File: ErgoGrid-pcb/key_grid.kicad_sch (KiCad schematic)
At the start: 0 parts

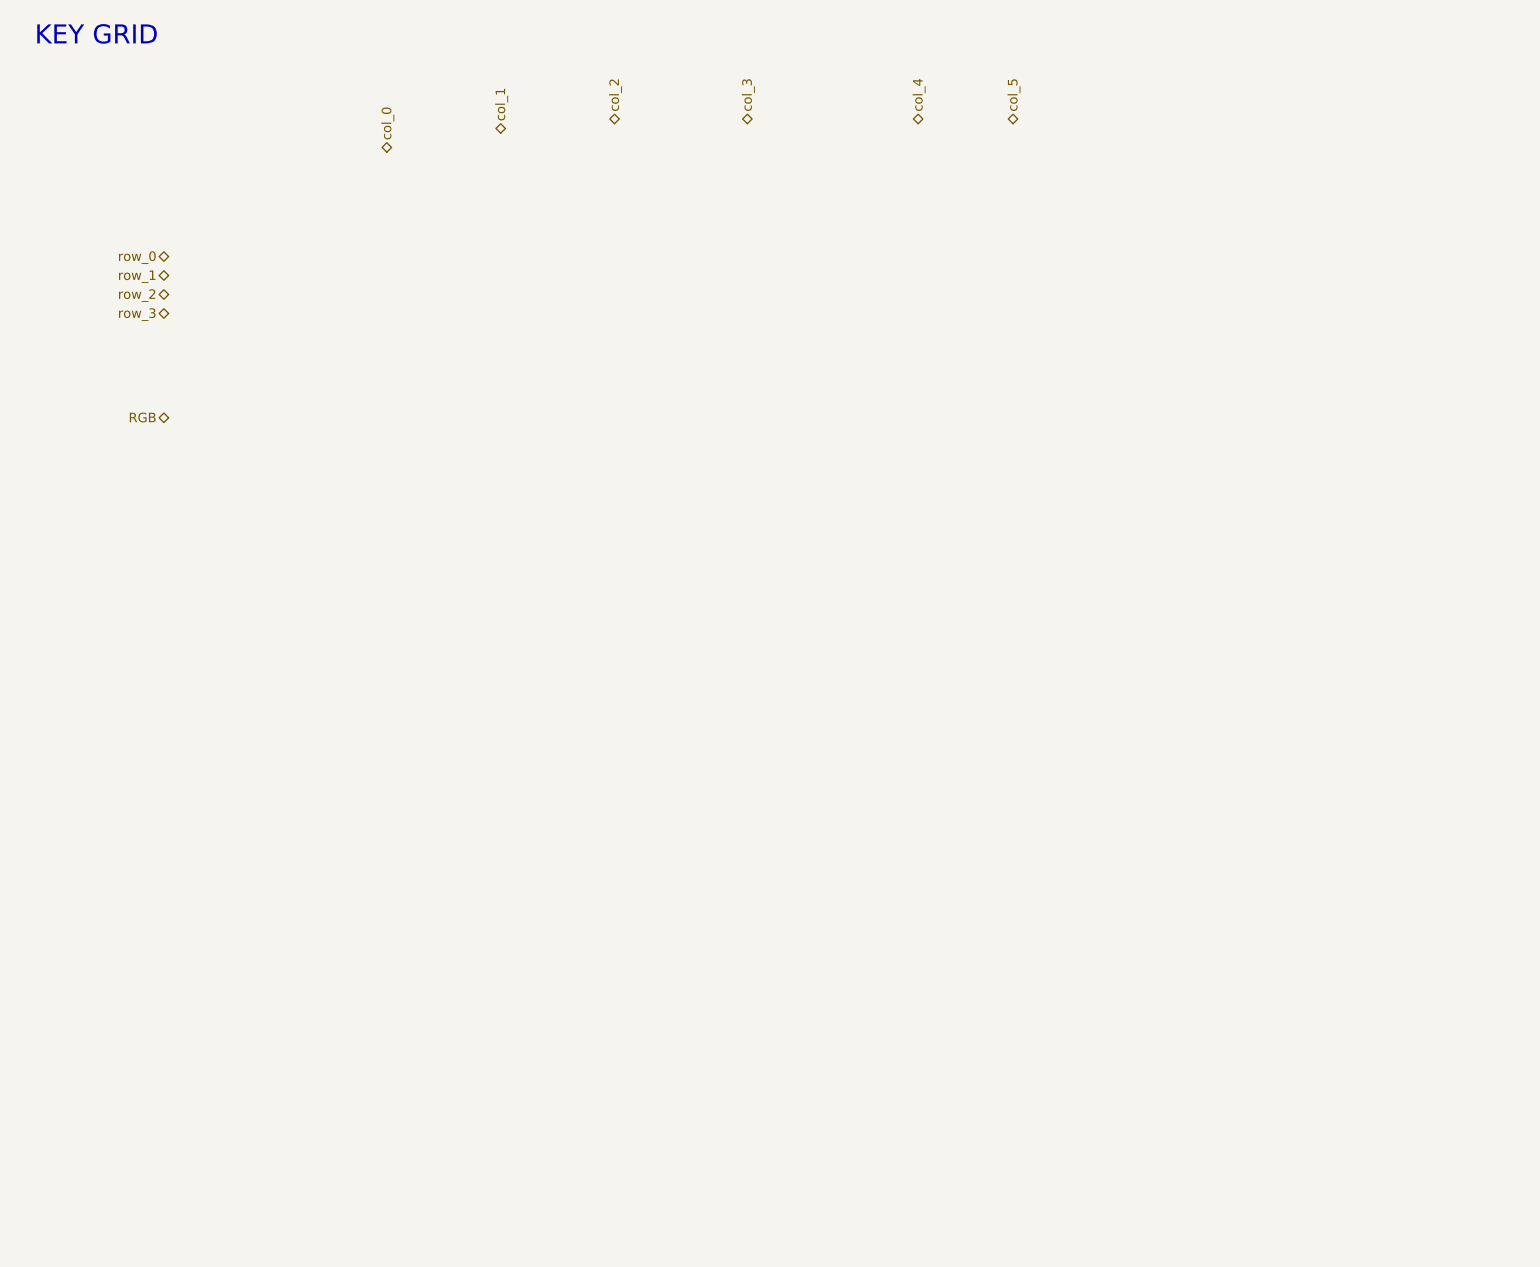
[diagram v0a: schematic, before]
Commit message: pcb: add key and RGB grids to schematic
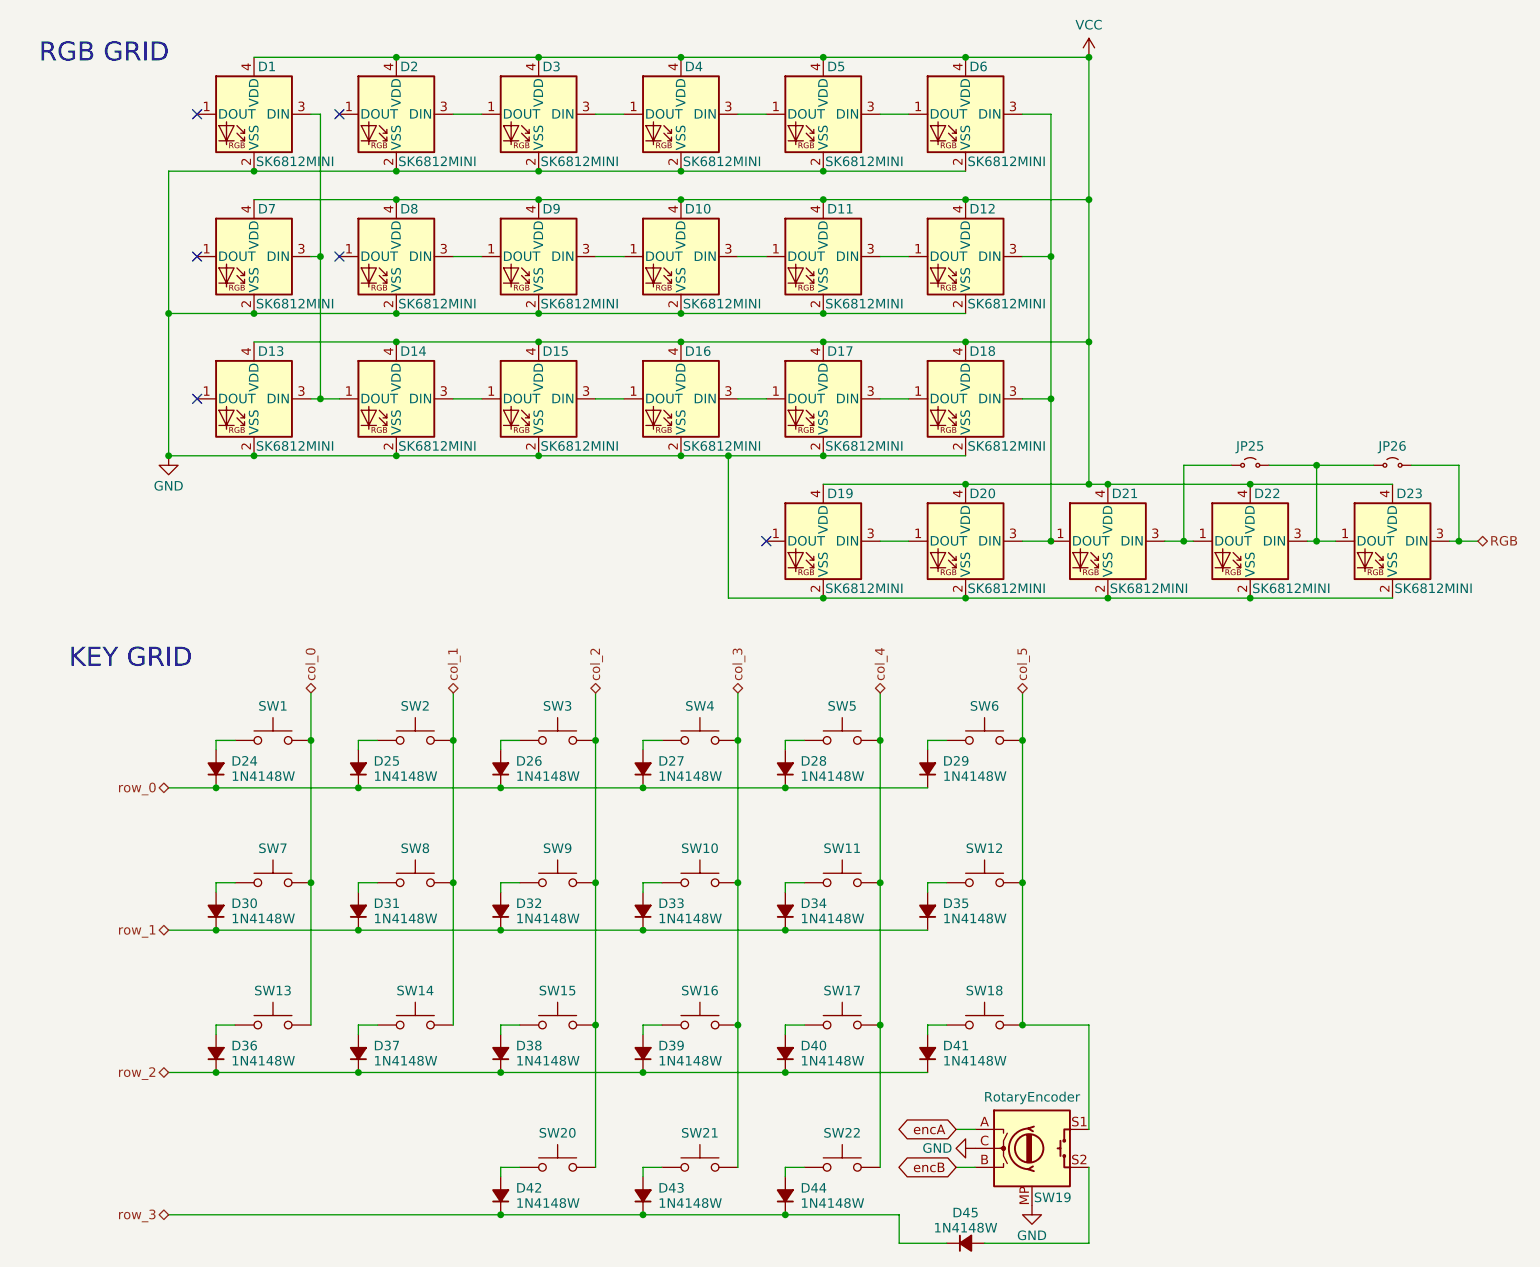
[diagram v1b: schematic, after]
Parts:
- added D1, D10, D11, D12, D13, D14, D15, D16, D17, D18, D19, D2, D20, D21, D22, D23, D3, D4, D5, D6, D7, D8, D9: SK6812MINI, LED_SMD:LED_SK6812MINI_PLCC4_3.5x3.5mm_P1.75mm, symbol SK6812MINI:SK6812MINI
- added D24, D25, D26, D27, D28, D29, D30, D31, D32, D33, D34, D35, D36, D37, D38, D39, D40, D41, D42, D43, D44, D45: 1N4148W, symbol D_Small_Filled:D_Small_Filled
- added JP25: EncBot, symbol Jumper_2_Small_Open:Jumper_2_Small_Open
- added JP26: EncTop, symbol Jumper_2_Small_Open:Jumper_2_Small_Open
- added SW1, SW10, SW11, SW12, SW13, SW14, SW15, SW16, SW17, SW18, SW2, SW20, SW21, SW22, SW3, SW4, SW5, SW6, SW7, SW8, SW9: SW_Push, symbol SW_Push:SW_Push
- added SW19: RotaryEncoder, symbol RotaryEncoder_Switch_MP:RotaryEncoder_Switch_MP
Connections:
- net RGB: now also D23.3 (DIN), JP26.2 (B)
- net col_0: now also SW1.2, SW13.2, SW7.2
- net col_1: now also SW14.2, SW2.2, SW8.2
- net col_2: now also SW15.2, SW20.2, SW3.2, SW9.2
- net col_3: now also SW10.2, SW16.2, SW21.2, SW4.2
- net col_4: now also SW11.2, SW17.2, SW22.2, SW5.2
- net col_5: now also SW12.2, SW18.2, SW19.S1, SW6.2
- net row_0: now also D24.1 (K), D25.1 (K), D26.1 (K), D27.1 (K), D28.1 (K), D29.1 (K)
- net row_1: now also D30.1 (K), D31.1 (K), D32.1 (K), D33.1 (K), D34.1 (K), D35.1 (K)
- net row_2: now also D36.1 (K), D37.1 (K), D38.1 (K), D39.1 (K), D40.1 (K), D41.1 (K)
- net row_3: now also D42.1 (K), D43.1 (K), D44.1 (K), D45.1 (K)
- new net: D22.3 (DIN), D23.1 (DOUT), JP25.2 (B), JP26.1 (A)
- new net: D33.2 (A), SW10.1
- new net: D45.2 (A), SW19.S2
- new net: D17.3 (DIN), D18.1 (DOUT)
- new net: D12.3 (DIN), D18.3 (DIN), D20.3 (DIN), D21.1 (DOUT), D6.3 (DIN)
- new net: D37.2 (A), SW14.1
- new net: D2.3 (DIN), D3.1 (DOUT)
- new net: D21.3 (DIN), D22.1 (DOUT), JP25.1 (A)
- new net: D3.3 (DIN), D4.1 (DOUT)
- new net: D4.3 (DIN), D5.1 (DOUT)
- new net: D30.2 (A), SW7.1
- new net: D40.2 (A), SW17.1
- new net: D43.2 (A), SW21.1
- new net: D29.2 (A), SW6.1
- new net: D25.2 (A), SW2.1
- new net: D36.2 (A), SW13.1
- new net: D26.2 (A), SW3.1
- new net: D34.2 (A), SW11.1
- new net: D44.2 (A), SW22.1
- new net: D24.2 (A), SW1.1
- new net: D38.2 (A), SW15.1
- new net: D1.3 (DIN), D13.3 (DIN), D14.1 (DOUT), D7.3 (DIN)
- new net: D11.3 (DIN), D12.1 (DOUT)
- new net: D5.3 (DIN), D6.1 (DOUT)
- new net: D32.2 (A), SW9.1
- new net: D31.2 (A), SW8.1
- new net: D14.3 (DIN), D15.1 (DOUT)
- new net: D15.3 (DIN), D16.1 (DOUT)
- new net: D10.1 (DOUT), D9.3 (DIN)
- new net: D10.3 (DIN), D11.1 (DOUT)
- new net: D35.2 (A), SW12.1
- new net: D16.3 (DIN), D17.1 (DOUT)
- new net: D28.2 (A), SW5.1
- new net: D41.2 (A), SW18.1
- new net: D8.3 (DIN), D9.1 (DOUT)
- new net: D39.2 (A), SW16.1
- new net: D19.3 (DIN), D20.1 (DOUT)
- new net: D27.2 (A), SW4.1
- new net: D42.2 (A), SW20.1
- new net GND: D1.2 (VSS), D10.2 (VSS), D11.2 (VSS), D12.2 (VSS), D13.2 (VSS), D14.2 (VSS), D15.2 (VSS), D16.2 (VSS), D17.2 (VSS), D18.2 (VSS), D19.2 (VSS), D2.2 (VSS), D20.2 (VSS), D21.2 (VSS), D22.2 (VSS), D23.2 (VSS), D3.2 (VSS), D4.2 (VSS), D5.2 (VSS), D6.2 (VSS), D7.2 (VSS), D8.2 (VSS), D9.2 (VSS), SW19.C, SW19.MP
- new net VCC: D1.4 (VDD), D10.4 (VDD), D11.4 (VDD), D12.4 (VDD), D13.4 (VDD), D14.4 (VDD), D15.4 (VDD), D16.4 (VDD), D17.4 (VDD), D18.4 (VDD), D19.4 (VDD), D2.4 (VDD), D20.4 (VDD), D21.4 (VDD), D22.4 (VDD), D23.4 (VDD), D3.4 (VDD), D4.4 (VDD), D5.4 (VDD), D6.4 (VDD), D7.4 (VDD), D8.4 (VDD), D9.4 (VDD)
- new net encA: SW19.A
- new net encB: SW19.B
- no-connect marks 0 -> 6
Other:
- note added: "RGB GRID"

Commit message: pcb: almost done with schematic
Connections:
- net encA renamed EncA
- net encB renamed EncB
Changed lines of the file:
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@@
 		)
 	)
-	(global_label "encA"
+	(global_label "EncA"
 		(shape bidirectional)
 		(at 143.51 166.37 180)
@@
 		)
 		(property "Intersheetrefs" "${INTERSHEET_REFS}"
-			(at 134.9987 166.37 0)
+			(at 134.9383 166.37 0)
 			(hide yes)
 			(show_name no)
@@
 		)
 	)
-	(global_label "encB"
+	(global_label "EncB"
 		(shape bidirectional)
 		(at 143.51 171.45 180)
@@
 		)
 		(property "Intersheetrefs" "${INTERSHEET_REFS}"
-			(at 134.8173 171.45 0)
+			(at 134.7569 171.45 0)
 			(hide yes)
 			(show_name no)

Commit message: pcb: complete schematic
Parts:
- JP37: renamed from JP25; footprint (none) -> Jumper:SolderJumper-2_P1.3mm_Open_TrianglePad1.0x1.5mm
- JP38: renamed from JP26; footprint (none) -> Jumper:SolderJumper-2_P1.3mm_Open_TrianglePad1.0x1.5mm
- renumbered SW19 to RE1, SW20 to SW19, SW21 to SW20, SW22 to SW21
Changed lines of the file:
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@@
 		(in_pos_files yes)
 		(dnp no)
-		(property "Reference" "JP26"
+		(property "Reference" "JP38"
 			(at 201.93 74.93 0)
 			(show_name no)
@@
 			)
 		)
-		(property "Footprint" ""
+		(property "Footprint" "Jumper:SolderJumper-2_P1.3mm_Open_TrianglePad1.0x1.5mm"
 			(at 201.93 77.47 0)
 			(hide yes)
@@
 			(project "ErgoGrid-pcb"
 				(path "/74a956b4-c88c-4954-9f37-5a65ad3d3678/0b5705a6-92dd-47ca-aedd-78d65c23ceb0"
-					(reference "JP26")
+					(reference "JP38")
 					(unit 1)
 				)
@@
 		(in_pos_files yes)
 		(dnp no)
-		(property "Reference" "#PWR06"
+		(property "Reference" "#PWR028"
 			(at 38.1 82.55 0)
 			(hide yes)
@@
 			(project "ErgoGrid-pcb"
 				(path "/74a956b4-c88c-4954-9f37-5a65ad3d3678/0b5705a6-92dd-47ca-aedd-78d65c23ceb0"
-					(reference "#PWR06")
+					(reference "#PWR028")
 					(unit 1)
 				)
@@
 		(in_pos_files yes)
 		(dnp no)
-		(property "Reference" "SW21"
+		(property "Reference" "SW20"
 			(at 109.22 166.878 0)
 			(show_name no)
@@
 			(project "ErgoGrid-pcb"
 				(path "/74a956b4-c88c-4954-9f37-5a65ad3d3678/0b5705a6-92dd-47ca-aedd-78d65c23ceb0"
-					(reference "SW21")
+					(reference "SW20")
 					(unit 1)
 				)
@@
 		(in_pos_files yes)
 		(dnp no)
-		(property "Reference" "SW22"
+		(property "Reference" "SW21"
 			(at 128.27 166.878 0)
 			(show_name no)
@@
 			(project "ErgoGrid-pcb"
 				(path "/74a956b4-c88c-4954-9f37-5a65ad3d3678/0b5705a6-92dd-47ca-aedd-78d65c23ceb0"
-					(reference "SW22")
+					(reference "SW21")
 					(unit 1)
 				)
@@
 		(in_pos_files yes)
 		(dnp no)
-		(property "Reference" "JP25"
+		(property "Reference" "JP37"
 			(at 182.88 74.93 0)
 			(show_name no)
@@
 			)
 		)
-		(property "Footprint" ""
+		(property "Footprint" "Jumper:SolderJumper-2_P1.3mm_Open_TrianglePad1.0x1.5mm"
 			(at 182.88 77.47 0)
 			(hide yes)
@@
 			(project "ErgoGrid-pcb"
 				(path "/74a956b4-c88c-4954-9f37-5a65ad3d3678/0b5705a6-92dd-47ca-aedd-78d65c23ceb0"
-					(reference "JP25")
+					(reference "JP37")
 					(unit 1)
 				)
@@
 		(in_pos_files yes)
 		(dnp no)
-		(property "Reference" "#PWR05"
+		(property "Reference" "#PWR027"
 			(at 161.29 26.67 0)
 			(hide yes)
@@
 			(project "ErgoGrid-pcb"
 				(path "/74a956b4-c88c-4954-9f37-5a65ad3d3678/0b5705a6-92dd-47ca-aedd-78d65c23ceb0"
-					(reference "#PWR05")
+					(reference "#PWR027")
 					(unit 1)
 				)
@@
 		(in_pos_files yes)
 		(dnp no)
-		(property "Reference" "SW19"
+		(property "Reference" "RE1"
 			(at 153.924 175.514 0)
 			(show_name no)
@@
 			(project "ErgoGrid-pcb"
 				(path "/74a956b4-c88c-4954-9f37-5a65ad3d3678/0b5705a6-92dd-47ca-aedd-78d65c23ceb0"
-					(reference "SW19")
+					(reference "RE1")
 					(unit 1)
 				)
@@
 		(in_pos_files yes)
 		(dnp no)
-		(property "Reference" "#PWR07"
+		(property "Reference" "#PWR029"
 			(at 139.7 168.91 0)
 			(hide yes)
@@
 			(project "ErgoGrid-pcb"
 				(path "/74a956b4-c88c-4954-9f37-5a65ad3d3678/0b5705a6-92dd-47ca-aedd-78d65c23ceb0"
-					(reference "#PWR07")
+					(reference "#PWR029")
 					(unit 1)
 				)
@@
 		(in_pos_files yes)
 		(dnp no)
-		(property "Reference" "#PWR08"
+		(property "Reference" "#PWR030"
 			(at 153.67 182.88 0)
 			(hide yes)
@@
 			(project "ErgoGrid-pcb"
 				(path "/74a956b4-c88c-4954-9f37-5a65ad3d3678/0b5705a6-92dd-47ca-aedd-78d65c23ceb0"
-					(reference "#PWR08")
+					(reference "#PWR030")
 					(unit 1)
 				)
@@
 		(in_pos_files yes)
 		(dnp no)
-		(property "Reference" "SW20"
+		(property "Reference" "SW19"
 			(at 90.17 166.878 0)
 			(show_name no)
@@
 			(project "ErgoGrid-pcb"
 				(path "/74a956b4-c88c-4954-9f37-5a65ad3d3678/0b5705a6-92dd-47ca-aedd-78d65c23ceb0"
-					(reference "SW20")
+					(reference "SW19")
 					(unit 1)
 				)
